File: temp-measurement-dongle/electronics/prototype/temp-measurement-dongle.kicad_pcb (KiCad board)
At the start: 2 copper layers, 70.3 x 67.5 mm, 76 parts, among them J1 USB2UART, J2 1.47 IPS LCD, J3 ConnBattery, J4 RTD_PT100, Q1 SS8050, Q2 SS8050, Q3 SS8050, SW1 RST, SW2 IN1, SW3 Boot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

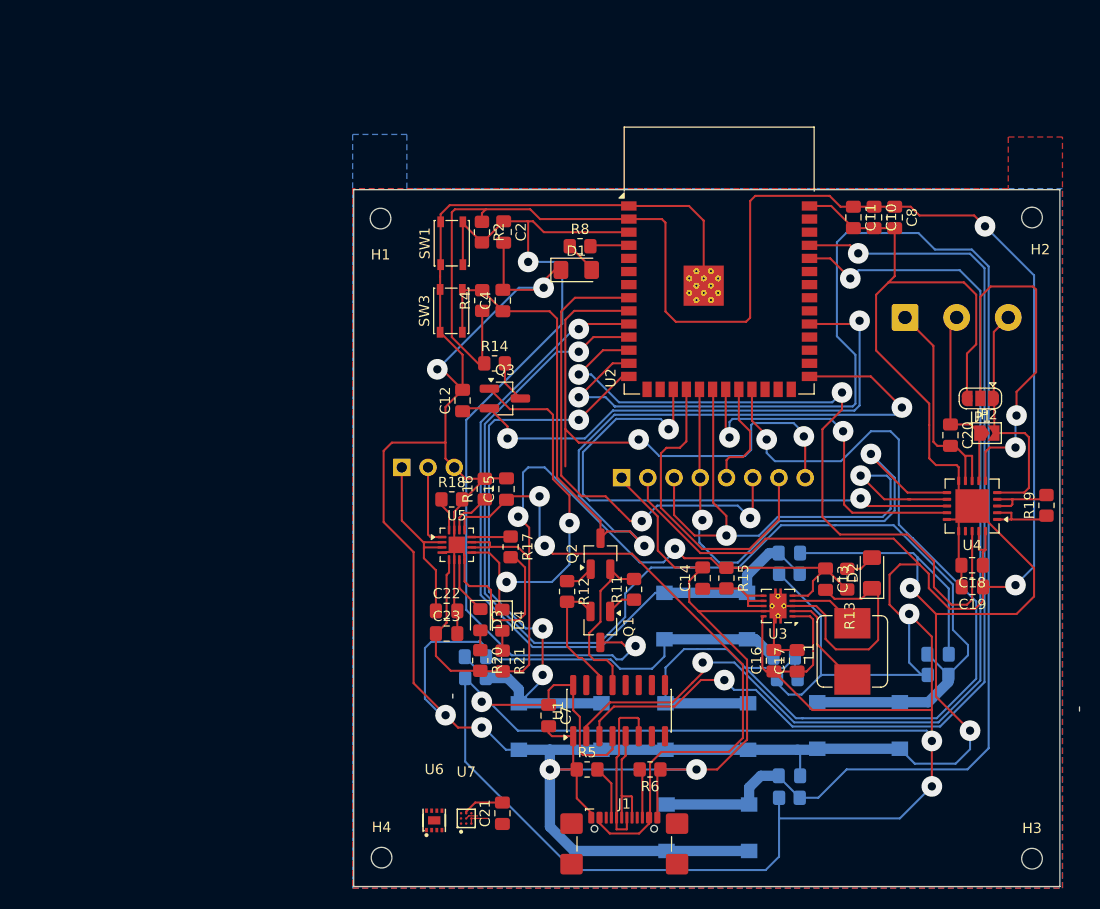
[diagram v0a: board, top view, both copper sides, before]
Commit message: feat(tmd): update schematic to use fuel gauge bq27421
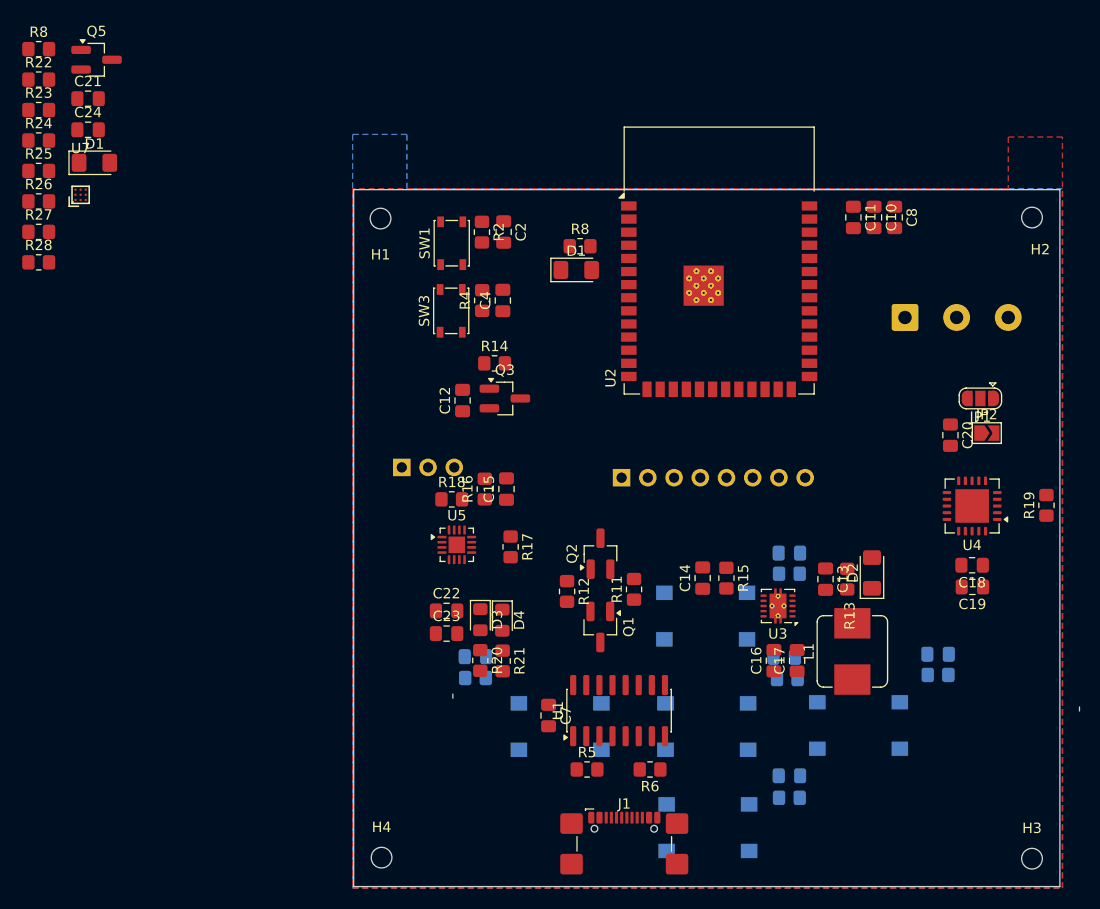
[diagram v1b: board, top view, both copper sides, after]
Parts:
- removed U6: MAX17048G+T10, easyeda2kicad:TDFN-8_L2.0-W2.0-P0.50-BL-EP1.2
- added C24: 100nF, Capacitor_SMD:C_0805_2012Metric_Pad1.18x1.45mm_HandSolder, F.Cu at (75.9, 61.8)
- added D1: INDICATOR, LED_SMD:LED_1206_3216Metric_Pad1.42x1.75mm_HandSolder, F.Cu at (76.5, 65.0)
- added Q5: SS8050, Package_TO_SOT_SMD:SOT-23_Handsoldering, F.Cu at (76.7, 55.0)
- added R22: 4K7, Resistor_SMD:R_0805_2012Metric_Pad1.20x1.40mm_HandSolder, F.Cu at (71.1, 56.9)
- added R23: 4K7, Resistor_SMD:R_0805_2012Metric_Pad1.20x1.40mm_HandSolder, F.Cu at (71.1, 59.9)
- added R24: 10k, Resistor_SMD:R_0805_2012Metric_Pad1.20x1.40mm_HandSolder, F.Cu at (71.1, 62.8)
- added R25: 10K, Resistor_SMD:R_0805_2012Metric_Pad1.20x1.40mm_HandSolder, F.Cu at (71.1, 65.8)
- added R26: 10K, Resistor_SMD:R_0805_2012Metric_Pad1.20x1.40mm_HandSolder, F.Cu at (71.1, 68.7)
- added R27: 1k, Resistor_SMD:R_0805_2012Metric_Pad1.20x1.40mm_HandSolder, F.Cu at (71.1, 71.7)
- added R28: 10k, Resistor_SMD:R_0805_2012Metric_Pad1.20x1.40mm_HandSolder, F.Cu at (71.1, 74.6)
- added R8: 1k, Resistor_SMD:R_0805_2012Metric_Pad1.20x1.40mm_HandSolder, F.Cu at (71.1, 54.0)
- C21: value 100nF -> 0.47uF
- U7: value BQ27220YZFR -> BQ27421YZFR-G1A; footprint easyeda2kicad:DSBGA-9_L1.7-W1.6-R3-C3-P0.50-BL -> easyeda2kicad:DSBGA-9_L1.5-W1.5-R3-C3-P0.50-BL
- moved C21 80.0 mm to (75.9, 58.8), turned to 0 degrees
- moved U7 71.0 mm to (75.2, 68.1)
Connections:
- C21 pad 1: GND -> Net-(U7-VDD)
- C21 pad 2: /bqvdd -> GND
- U2 pad 32: unconnected-(U2-IO39-Pad32) -> /GPOUT
- U2 pad 38: unconnected-(U2-IO2-Pad38) -> /I2C_SCL
- U2 pad 39: unconnected-(U2-IO1-Pad39) -> /I2C_SDA
- U2 pad 5: unconnected-(U2-IO5-Pad5) -> /MOSI2
- U2 pad 6: unconnected-(U2-IO6-Pad6) -> /SCK2
- U2 pad 7: unconnected-(U2-IO7-Pad7) -> /MISO2
- U4 pad 11: /MOSI -> /MOSI2
- U4 pad 12: /SCK -> /SCK2
- U4 pad 14: /MISO -> /MISO2
- U7 pad A1: /bqbypassed -> Net-(Q5-B)
- U7 pad A2: /bqbypassed -> /I2C_SCL
- U7 pad A3: /bqbypassed -> /I2C_SDA
- U7 pad B3: /bqvdd -> Net-(U7-VDD)
- U7 pad C1: /bqbypassed -> GND
- U7 pad C2: /bqbypassed -> +3.3V
- U7 pad C3: /bqbypassed -> +BATT
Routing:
- net GND: track 545.8 -> 0.00 mm, vias 8 -> 0
- net +3.3V: track 418.8 -> 0.00 mm, vias 6 -> 0
- net /IN3: track 149.2 -> 0.00 mm, vias 1 -> 0
- net /IN2: track 116.9 -> 0.00 mm, vias 1 -> 0
- net /RXD0: track 102.6 -> 0.00 mm, vias 2 -> 0
- net /TXD0: track 102.0 -> 0.00 mm, vias 2 -> 0
- net /IN5: track 101.9 -> 0.00 mm, vias 1 -> 0
- net /IO0: track 98.6 -> 0.00 mm, vias 2 -> 0
- net VDD: track 89.8 -> 0.00 mm, vias 2 -> 0
- net /EN: track 89.3 -> 0.00 mm, vias 2 -> 0
- net /IN1: track 73.6 -> 0.00 mm, vias 1 -> 0
- net /MAX31865DRDY: track 72.0 -> 0.00 mm, vias 2 -> 0
- net VBUS: track 67.4 -> 0.00 mm, vias 2 -> 0
- net /IN4: track 62.4 -> 0.00 mm, vias 3 -> 0
- net /SCK: track 56.6 -> 0.00 mm, vias 2 -> 0
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
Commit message: chore: move libraries to mkl
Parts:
- R19: value 400 1% -> 430 1%
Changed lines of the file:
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@@
 			)
 		)
-		(property "KiLib_Generator" "SMD_2terminal_chip_molded"
-			(at 0 0 0)
-			(layer "F.SilkS")
-			(hide yes)
-			(effects
-				(font
-					(size 1 1)
-					(thickness 0.15)
-				)
-			)
-		)
 		(property ki_fp_filters "C_*")
 		(sheetname "/")
@@
 			)
 		)
-		(property "KiLib_Generator" "SMD_2terminal_chip_molded"
-			(at 0 0 0)
-			(layer "F.SilkS")
-			(hide yes)
-			(effects
-				(font
-					(size 1 1)
-					(thickness 0.15)
-				)
-			)
-		)
 		(property ki_fp_filters "R_*")
 		(sheetname "/")
@@
 			)
 		)
-		(property "KiLib_Generator" "SMD_2terminal_chip_molded"
-			(at 0 0 0)
-			(layer "F.SilkS")
-			(hide yes)
-			(effects
-				(font
-					(size 1 1)
-					(thickness 0.15)
-				)
-			)
-		)
 		(property ki_fp_filters "R_*")
 		(sheetname "/")
@@
 			)
 		)
-		(property "KiLib_Generator" "SMD_2terminal_chip_molded"
-			(at 0 0 0)
-			(layer "F.SilkS")
-			(hide yes)
-			(effects
-				(font
-					(size 1 1)
-					(thickness 0.15)
-				)
-			)
-		)
 		(property ki_fp_filters "LED* LED_SMD:* LED_THT:*")
 		(sheetname "/")
@@
 			)
 		)
-		(property "KiLib_Generator" "SMD_2terminal_chip_molded"
-			(at 0 0 0)
-			(layer "F.SilkS")
-			(hide yes)
-			(effects
-				(font
-					(size 1 1)
-					(thickness 0.15)
-				)
-			)
-		)
 		(property ki_fp_filters "R_*")
 		(sheetname "/")
@@
 			)
 		)
-		(property "KiLib_Generator" "SMD_2terminal_chip_molded"
-			(at 0 0 0)
-			(layer "F.SilkS")
-			(hide yes)
-			(effects
-				(font
-					(size 1 1)
-					(thickness 0.15)
-				)
-			)
-		)
 		(property ki_fp_filters "R_*")
 		(sheetname "/")
@@
 			)
 		)
-		(property "Value" "400 1%"
+		(property "Value" "430 1%"
 			(at 0 1.65 90)
 			(layer "F.Fab")
@@
 			)
 		)
+		(property "Field5" ""
+			(at 0 0 90)
+			(unlocked yes)
+			(layer "F.Fab")
+			(hide yes)
+			(effects
+				(font
+					(size 1 1)
+					(thickness 0.15)
+				)
+			)
+		)
 		(property ki_fp_filters "R_*")
 		(sheetname "/")
@@
 			)
 		)
-		(property "KiLib_Generator" "SMD_2terminal_chip_molded"
-			(at 0 0 0)
-			(layer "F.SilkS")
-			(hide yes)
-			(effects
-				(font
-					(size 1 1)
-					(thickness 0.15)
-				)
-			)
-		)
 		(property ki_fp_filters "C_*")
 		(sheetname "/")
@@
 			)
 		)
-		(property "KiLib_Generator" "SMD_2terminal_chip_molded"
-			(at 0 0 0)
-			(layer "F.SilkS")
-			(hide yes)
-			(effects
-				(font
-					(size 1 1)
-					(thickness 0.15)
-				)
-			)
-		)
 		(property ki_fp_filters "R_*")
 		(sheetname "/")
@@
 				(font
 					(size 1.27 1.27)
+					(thickness 0.15)
 				)
 			)
@@
 			)
 		)
-		(property "KiLib_Generator" "SMD_2terminal_chip_molded"
-			(at 0 0 0)
-			(layer "F.SilkS")
-			(hide yes)
-			(effects
-				(font
-					(size 1 1)
-					(thickness 0.15)
-				)
-			)
-		)
 		(property ki_fp_filters "R_*")
 		(sheetname "/")
@@
 			)
 		)
-		(property "KiLib_Generator" "SMD_2terminal_chip_molded"
-			(at 0 0 0)
-			(layer "F.SilkS")
-			(hide yes)
-			(effects
-				(font
-					(size 1 1)
-					(thickness 0.15)
-				)
-			)
-		)
 		(property ki_fp_filters "R_*")
 		(sheetname "/")
@@
 				)
 			)
-		)
-		(property "KiLib_Generator" "SMD_2terminal_chip_molded"
-			(at 0 0 0)
-			(layer "F.SilkS")
-			(hide yes)
-			(effects
-				(font
-					(size 1 1)
-					(thickness 0.15)
-				)
-			)
